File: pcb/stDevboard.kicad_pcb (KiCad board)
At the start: 4 copper layers, 50 x 100 mm, 149 parts, among them IC1 MPM3610GQV-Z, IC2 IRFR9014PBF, IC3 ICM-45686, IC4 ICM-45686, IC5 MMC5983MA, IC6 AT25SF041B-SSHB-B, J1 USB_C_Receptacle_USB2.0_16P, J10 Micro_SD_Card_Det2, J2 USB_C_Receptacle_USB2.0_16P, J4 Conn_02x03_Top_Bottom, J7 73412-0114, J8 73412-0114, Q1 DMN3404L, Q2 MMBT2222A, Q3 DMN3404L, Q4 DMN3404L, Q5 DMN3404L, Q6 DMN3404L, Q7 DMN3404L, Q8 MMBT2222A, U1 BMP581, U2 H3LIS331DLTR, U3 MAX-M10S, U4 STM32U585CIUxQ, U5 STM32U073CCUx, Y1 ECS-TXO-25CSMV-320-AM-TR, Y2 ECS-160-8-36B2-CKM-TR, Y3 CM7V-T1A-32.768KHZ, Y4 CM7V-T1A-32.768KHZ

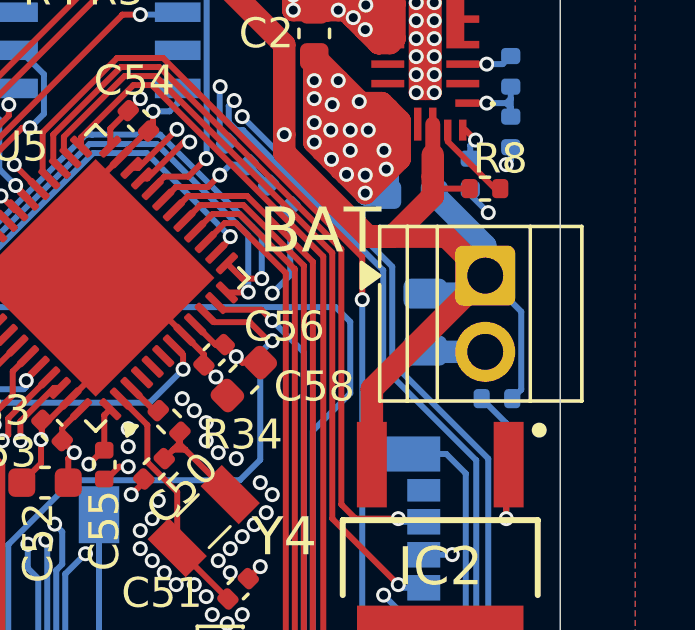
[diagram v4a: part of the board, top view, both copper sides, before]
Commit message: started making bom - changed some stuff for compatibility with it
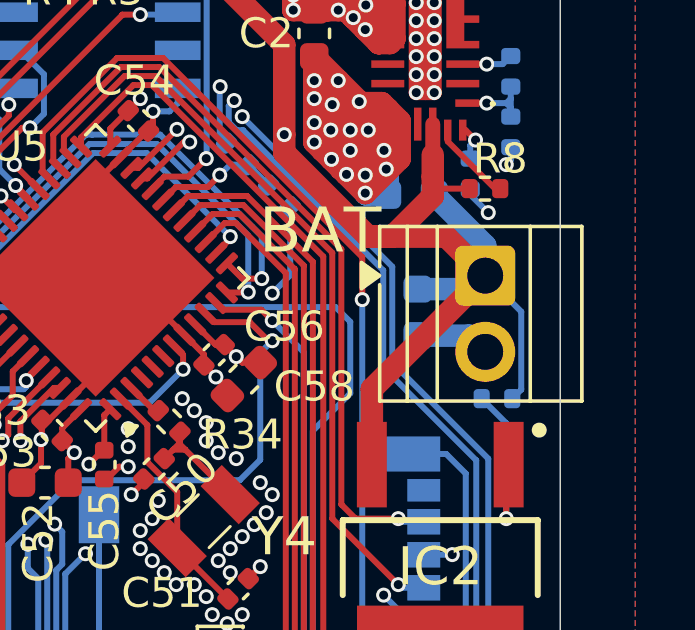
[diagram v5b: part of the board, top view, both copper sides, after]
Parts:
- C1: footprint Capacitor_SMD:C_0805_2012Metric -> Capacitor_SMD:C_0603_1608Metric
- moved C1 0.41 mm to (145.2, 95.5)
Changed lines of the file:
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@@
 		)
 	)
-	(footprint "Capacitor_SMD:C_0805_2012Metric"
+	(footprint "Capacitor_SMD:C_0603_1608Metric"
 		(layer "B.Cu")
-		(at 145.5 95.85 -90)
-		(descr "Capacitor SMD 0805 (2012 Metric), square (rectangular) end terminal, IPC-7351 nominal, (Body size source: IPC-SM-782 page 76, https://www.pcb-3d.com/wordpress/wp-content/uploads/ipc-sm-782a_amendment_1_and_2.pdf, https://docs.google.com/spreadsheets/d/1BsfQQcO9C6DZCsRaXUlFlo91Tg2WpOkGARC1WS5S8t0/edit?usp=sharing), generated with kicad-footprint-generator")
+		(at 145.25 95.525 -90)
+		(descr "Capacitor SMD 0603 (1608 Metric), square (rectangular) end terminal, IPC-7351 nominal, (Body size source: IPC-SM-782 page 76, https://www.pcb-3d.com/wordpress/wp-content/uploads/ipc-sm-782a_amendment_1_and_2.pdf), generated with kicad-footprint-generator")
 		(tags "capacitor")
 		(property "Reference" "C1"
-			(at 0 1.68 90)
+			(at 0 1.43 90)
 			(layer "B.SilkS")
 			(effects
 				(font
 					(size 1 1)
-					(thickness 0.16)
+					(thickness 0.15)
 				)
 				(justify mirror)
@@
 		)
 		(property "Value" "100uF"
-			(at 0 -1.68 90)
+			(at 0 -1.43 90)
 			(layer "B.Fab")
 			(effects
@@
 			)
 		)
-		(property "Datasheet" "~"
+		(property "Datasheet" ""
 			(at 0 0 90)
 			(layer "B.Fab")
@@
 			)
 		)
-		(property "Description" "Unpolarized capacitor"
+		(property "Description" ""
 			(at 0 0 90)
 			(layer "B.Fab")
@@
 		(attr smd)
 		(fp_line
-			(start -0.261252 0.735)
-			(end 0.261252 0.735)
+			(start -0.14058 0.51)
+			(end 0.14058 0.51)
 			(stroke
 				(width 0.12)
@@
 		)
 		(fp_line
-			(start -0.261252 -0.735)
-			(end 0.261252 -0.735)
+			(start -0.14058 -0.51)
+			(end 0.14058 -0.51)
 			(stroke
 				(width 0.12)
@@
 		)
 		(fp_line
-			(start -1.7 0.98)
-			(end 1.7 0.98)
+			(start -1.48 0.73)
+			(end 1.48 0.73)
 			(stroke
 				(width 0.05)
@@
 		)
 		(fp_line
-			(start 1.7 0.98)
-			(end 1.7 -0.98)
+			(start 1.48 0.73)
+			(end 1.48 -0.73)
 			(stroke
 				(width 0.05)
@@
 		)
 		(fp_line
-			(start -1.7 -0.98)
-			(end -1.7 0.98)
+			(start -1.48 -0.73)
+			(end -1.48 0.73)
 			(stroke
 				(width 0.05)
@@
 		)
 		(fp_line
-			(start 1.7 -0.98)
-			(end -1.7 -0.98)
+			(start 1.48 -0.73)
+			(end -1.48 -0.73)
 			(stroke
 				(width 0.05)
@@
 		)
 		(fp_line
-			(start -1 0.625)
-			(end 1 0.625)
+			(start -0.8 0.4)
+			(end 0.8 0.4)
 			(stroke
 				(width 0.1)
@@
 		)
 		(fp_line
-			(start 1 0.625)
-			(end 1 -0.625)
+			(start 0.8 0.4)
+			(end 0.8 -0.4)
 			(stroke
 				(width 0.1)
@@
 		)
 		(fp_line
-			(start -1 -0.625)
-			(end -1 0.625)
+			(start -0.8 -0.4)
+			(end -0.8 0.4)
 			(stroke
 				(width 0.1)
@@
 		)
 		(fp_line
-			(start 1 -0.625)
-			(end -1 -0.625)
+			(start 0.8 -0.4)
+			(end -0.8 -0.4)
 			(stroke
 				(width 0.1)
@@
 			(effects
 				(font
-					(size 0.5 0.5)
-					(thickness 0.08)
+					(size 0.4 0.4)
+					(thickness 0.06)
 				)
 				(justify mirror)
@@
 		)
 		(pad "1" smd roundrect
-			(at -0.95 0 270)
-			(size 1 1.45)
+			(at -0.775 0 270)
+			(size 0.9 0.95)
 			(layers "B.Cu" "B.Mask" "B.Paste")
 			(roundrect_rratio 0.25)
@@
 		)
 		(pad "2" smd roundrect
-			(at 0.95 0 270)
-			(size 1 1.45)
+			(at 0.775 0 270)
+			(size 0.9 0.95)
 			(layers "B.Cu" "B.Mask" "B.Paste")
 			(roundrect_rratio 0.25)
@@
 		)
 		(embedded_fonts no)
-		(model "${KICAD9_3DMODEL_DIR}/Capacitor_SMD.3dshapes/C_0805_2012Metric.step"
+		(model "${KICAD9_3DMODEL_DIR}/Capacitor_SMD.3dshapes/C_0603_1608Metric.step"
 			(offset
 				(xyz 0 0 0)
@@
 	)
 	(segment
+		(start 145.25 96.3)
+		(end 146.96 96.3)
+		(width 0.75)
+		(layer "B.Cu")
+		(net 1)
+	)
+	(segment
 		(start 138.648 88.0155)
 		(end 138.6635 88)
@@
 	)
 	(segment
+		(start 146.96 96.3)
+		(end 147.5 96.84)
+		(width 0.75)
+		(layer "B.Cu")
+		(net 1)
+	)
+	(segment
 		(start 144.25 91.6)
 		(end 143.55 91.6)
@@
 	)
 	(segment
-		(start 147.5 96.84)
-		(end 145.54 96.84)
-		(width 0.75)
-		(layer "B.Cu")
-		(net 1)
-	)
-	(segment
 		(start 120.2 98)
 		(end 120.6 98.4)
@@
 	)
 	(segment
-		(start 145.54 96.84)
-		(end 145.5 96.8)
-		(width 0.75)
-		(layer "B.Cu")
-		(net 1)
-	)
-	(segment
 		(start 125.56 105.04)
 		(end 125.6 105)
@@
 	)
 	(segment
-		(start 146.9 94.9)
-		(end 147.5 94.3)
+		(start 145.25 94.75)
+		(end 147.05 94.75)
 		(width 0.75)
 		(layer "B.Cu")
@@
 	)
 	(segment
-		(start 148.701 95.501)
+		(start 147.05 94.75)
 		(end 147.5 94.3)
-		(width 0.2)
+		(width 0.75)
 		(layer "B.Cu")
 		(net 72)
 	)
 	(segment
-		(start 147.5 93.3)
-		(end 145.8 91.6)
-		(width 0.75)
+		(start 148.701 95.501)
+		(end 147.5 94.3)
+		(width 0.2)
 		(layer "B.Cu")
 		(net 72)
 	)
 	(segment
-		(start 145.5 94.9)
-		(end 146.9 94.9)
+		(start 147.5 93.3)
+		(end 145.8 91.6)
 		(width 0.75)
 		(layer "B.Cu")
